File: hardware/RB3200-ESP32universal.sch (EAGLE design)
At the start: 140 parts, among them IC2 7805, IC3 CP2102N-28, T1 BC337, T2 BC337, U1 ESP-WROOM-32, U2 UM18533, U3 ARDUINOR3-BPLACE, X1 USB-MICRO-B-BOTTOM

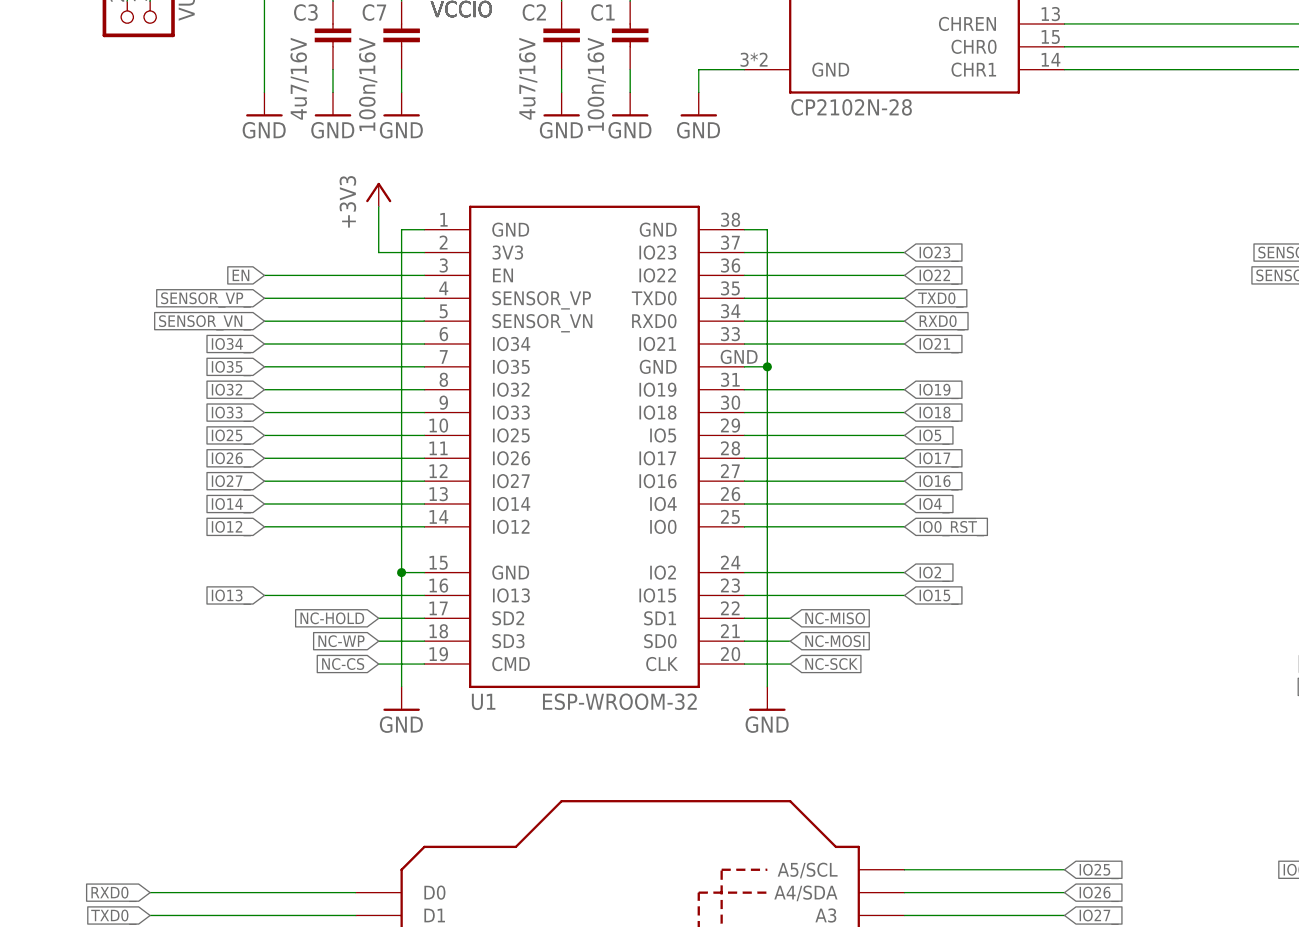
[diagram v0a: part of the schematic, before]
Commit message: Add enable pullup
This solves board flashing issues.
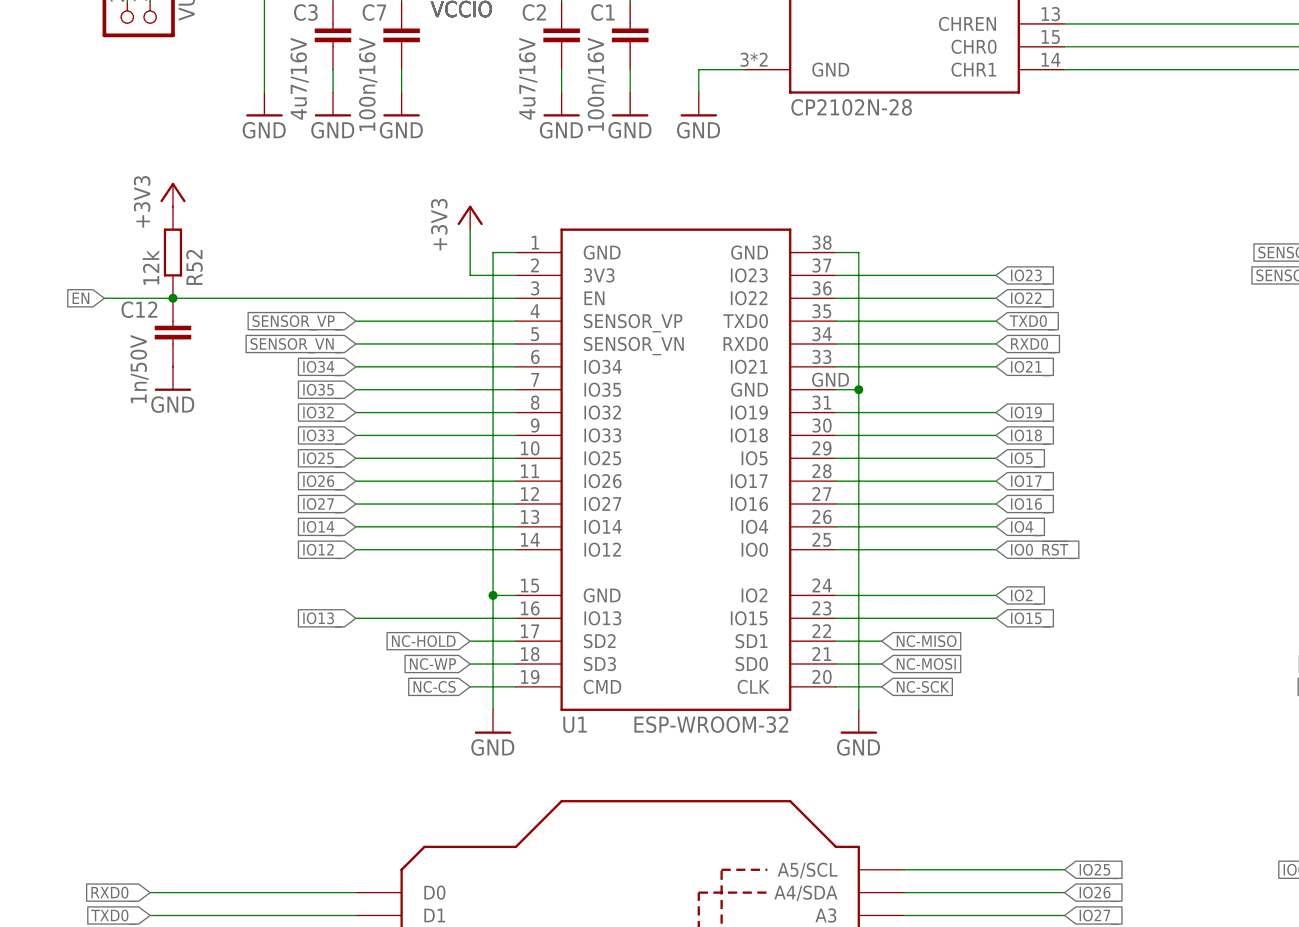
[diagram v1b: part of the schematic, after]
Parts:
- added C12: 1n/50V, rcl_upravena:C-EUC0603
- added R52: 12k, rcl_upravena:R-EU_R0603
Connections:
- net +3V3: now also R52.2
- net EN: now also C12.1, R52.1
- net GND: now also C12.2
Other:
- moved on the sheet: U1

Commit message: Change EN pullup value to simplify BOM
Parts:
- R52: value 12k -> 10k
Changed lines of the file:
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@@
 <grid distance="0.1" unitdist="inch" unit="inch" style="lines" multiple="1" display="no" altdistance="0.01" altunitdist="inch" altunit="inch"/>
 <layers>
-<layer number="1" name="Top" color="4" fill="1" visible="yes" active="no"/>
-<layer number="2" name="Route2" color="1" fill="3" visible="yes" active="no"/>
-<layer number="3" name="Route3" color="4" fill="3" visible="yes" active="no"/>
-<layer number="4" name="Route4" color="1" fill="4" visible="yes" active="no"/>
-<layer number="5" name="Route5" color="4" fill="4" visible="yes" active="no"/>
-<layer number="6" name="Route6" color="1" fill="8" visible="yes" active="no"/>
-<layer number="7" name="Route7" color="4" fill="8" visible="yes" active="no"/>
-<layer number="8" name="Route8" color="1" fill="2" visible="yes" active="no"/>
-<layer number="9" name="Route9" color="4" fill="2" visible="yes" active="no"/>
-<layer number="10" name="Route10" color="1" fill="7" visible="yes" active="no"/>
-<layer number="11" name="Route11" color="4" fill="7" visible="yes" active="no"/>
-<layer number="12" name="Route12" color="1" fill="5" visible="yes" active="no"/>
-<layer number="13" name="Route13" color="4" fill="5" visible="yes" active="no"/>
-<layer number="14" name="Route14" color="1" fill="6" visible="yes" active="no"/>
-<layer number="15" name="Route15" color="4" fill="6" visible="yes" active="no"/>
-<layer number="16" name="Bottom" color="1" fill="1" visible="yes" active="no"/>
-<layer number="17" name="Pads" color="2" fill="1" visible="yes" active="no"/>
-<layer number="18" name="Vias" color="2" fill="1" visible="yes" active="no"/>
-<layer number="19" name="Unrouted" color="6" fill="1" visible="yes" active="no"/>
-<layer number="20" name="Dimension" color="15" fill="1" visible="yes" active="no"/>
-<layer number="21" name="tPlace" color="7" fill="1" visible="yes" active="no"/>
-<layer number="22" name="bPlace" color="7" fill="1" visible="yes" active="no"/>
-<layer number="23" name="tOrigins" color="15" fill="1" visible="yes" active="no"/>
-<layer number="24" name="bOrigins" color="15" fill="1" visible="yes" active="no"/>
-<layer number="25" name="tNames" color="7" fill="1" visible="yes" active="no"/>
-<layer number="26" name="bNames" color="7" fill="1" visible="yes" active="no"/>
-<layer number="27" name="tValues" color="7" fill="1" visible="yes" active="no"/>
-<layer number="28" name="bValues" color="7" fill="1" visible="yes" active="no"/>
+<layer number="1" name="Top" color="4" fill="1" visible="no" active="no"/>
+<layer number="2" name="Route2" color="1" fill="3" visible="no" active="no"/>
+<layer number="3" name="Route3" color="4" fill="3" visible="no" active="no"/>
+<layer number="4" name="Route4" color="1" fill="4" visible="no" active="no"/>
+<layer number="5" name="Route5" color="4" fill="4" visible="no" active="no"/>
+<layer number="6" name="Route6" color="1" fill="8" visible="no" active="no"/>
+<layer number="7" name="Route7" color="4" fill="8" visible="no" active="no"/>
+<layer number="8" name="Route8" color="1" fill="2" visible="no" active="no"/>
+<layer number="9" name="Route9" color="4" fill="2" visible="no" active="no"/>
+<layer number="10" name="Route10" color="1" fill="7" visible="no" active="no"/>
+<layer number="11" name="Route11" color="4" fill="7" visible="no" active="no"/>
+<layer number="12" name="Route12" color="1" fill="5" visible="no" active="no"/>
+<layer number="13" name="Route13" color="4" fill="5" visible="no" active="no"/>
+<layer number="14" name="Route14" color="1" fill="6" visible="no" active="no"/>
+<layer number="15" name="Route15" color="4" fill="6" visible="no" active="no"/>
+<layer number="16" name="Bottom" color="1" fill="1" visible="no" active="no"/>
+<layer number="17" name="Pads" color="2" fill="1" visible="no" active="no"/>
+<layer number="18" name="Vias" color="2" fill="1" visible="no" active="no"/>
+<layer number="19" name="Unrouted" color="6" fill="1" visible="no" active="no"/>
+<layer number="20" name="Dimension" color="15" fill="1" visible="no" active="no"/>
+<layer number="21" name="tPlace" color="7" fill="1" visible="no" active="no"/>
+<layer number="22" name="bPlace" color="7" fill="1" visible="no" active="no"/>
+<layer number="23" name="tOrigins" color="15" fill="1" visible="no" active="no"/>
+<layer number="24" name="bOrigins" color="15" fill="1" visible="no" active="no"/>
+<layer number="25" name="tNames" color="7" fill="1" visible="no" active="no"/>
+<layer number="26" name="bNames" color="7" fill="1" visible="no" active="no"/>
+<layer number="27" name="tValues" color="7" fill="1" visible="no" active="no"/>
+<layer number="28" name="bValues" color="7" fill="1" visible="no" active="no"/>
 <layer number="29" name="tStop" color="7" fill="3" visible="no" active="no"/>
 <layer number="30" name="bStop" color="7" fill="6" visible="no" active="no"/>
@@
 <layer number="35" name="tGlue" color="7" fill="4" visible="no" active="no"/>
 <layer number="36" name="bGlue" color="7" fill="5" visible="no" active="no"/>
-<layer number="37" name="tTest" color="7" fill="1" visible="yes" active="no"/>
-<layer number="38" name="bTest" color="7" fill="1" visible="yes" active="no"/>
+<layer number="37" name="tTest" color="7" fill="1" visible="no" active="no"/>
+<layer number="38" name="bTest" color="7" fill="1" visible="no" active="no"/>
 <layer number="39" name="tKeepout" color="4" fill="11" visible="no" active="no"/>
 <layer number="40" name="bKeepout" color="1" fill="11" visible="no" active="no"/>
@@
 <layer number="44" name="Drills" color="7" fill="1" visible="no" active="no"/>
 <layer number="45" name="Holes" color="7" fill="1" visible="no" active="no"/>
-<layer number="46" name="Milling" color="3" fill="1" visible="yes" active="no"/>
-<layer number="47" name="Measures" color="7" fill="1" visible="yes" active="no"/>
-<layer number="48" name="Document" color="7" fill="1" visible="yes" active="no"/>
-<layer number="49" name="Reference" color="7" fill="1" visible="yes" active="no"/>
-<layer number="50" name="dxf" color="7" fill="1" visible="yes" active="no"/>
-<layer number="51" name="tDocu" color="7" fill="1" visible="yes" active="no"/>
-<layer number="52" name="bDocu" color="7" fill="1" visible="yes" active="no"/>
-<layer number="53" name="tGND_GNDA" color="7" fill="9" visible="yes" active="no"/>
-<layer number="54" name="bGND_GNDA" color="1" fill="9" visible="yes" active="no"/>
-<layer number="55" name="tPotisk" color="7" fill="1" visible="yes" active="no"/>
-<layer number="56" name="wert" color="7" fill="1" visible="yes" active="no"/>
-<layer number="57" name="tCAD" color="7" fill="1" visible="yes" active="no"/>
-<layer number="58" name="bNC" color="7" fill="1" visible="yes" active="no"/>
-<layer number="59" name="tCarbon" color="7" fill="1" visible="yes" active="no"/>
-<layer number="60" name="bCarbon" color="7" fill="1" visible="yes" active="no"/>
-<layer number="61" name="stand" color="7" fill="1" visible="yes" active="no"/>
+<layer number="46" name="Milling" color="3" fill="1" visible="no" active="no"/>
+<layer number="47" name="Measures" color="7" fill="1" visible="no" active="no"/>
+<layer number="48" name="Document" color="7" fill="1" visible="no" active="no"/>
+<layer number="49" name="Reference" color="7" fill="1" visible="no" active="no"/>
+<layer number="50" name="dxf" color="7" fill="1" visible="no" active="no"/>
+<layer number="51" name="tDocu" color="7" fill="1" visible="no" active="no"/>
+<layer number="52" name="bDocu" color="7" fill="1" visible="no" active="no"/>
+<layer number="53" name="tGND_GNDA" color="7" fill="9" visible="no" active="no"/>
+<layer number="54" name="bGND_GNDA" color="1" fill="9" visible="no" active="no"/>
+<layer number="55" name="tPotisk" color="7" fill="1" visible="no" active="no"/>
+<layer number="56" name="wert" color="7" fill="1" visible="no" active="no"/>
+<layer number="57" name="tCAD" color="7" fill="1" visible="no" active="no"/>
+<layer number="58" name="bNC" color="7" fill="1" visible="no" active="no"/>
+<layer number="59" name="tCarbon" color="7" fill="1" visible="no" active="no"/>
+<layer number="60" name="bCarbon" color="7" fill="1" visible="no" active="no"/>
+<layer number="61" name="stand" color="7" fill="1" visible="no" active="no"/>
 <layer number="90" name="Modules" color="5" fill="1" visible="no" active="yes"/>
 <layer number="91" name="Nets" color="2" fill="1" visible="yes" active="yes"/>
@@
 <part name="+3V15" library="supply1" deviceset="+3V3" device=""/>
 <part name="FRAME2" library="frames" deviceset="A3L-LOC" device=""/>
-<part name="R52" library="rcl_upravena" deviceset="R-EU_" device="R0603" value="12k"/>
+<part name="R52" library="rcl_upravena" deviceset="R-EU_" device="R0603" value="10k"/>
 <part name="C12" library="rcl_upravena" deviceset="C-EU" device="C0603" value="1n/50V"/>
 <part name="GND32" library="supply1" deviceset="GND" device=""/>

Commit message: Add order codes to the components.
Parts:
- !CTS, !DCD, !DSR, !DTR, !RESET, !RTS, !SUSPEND, CHR0, CHR1, CHREN, IO0/TXLED, IO1/RXLED, IO2/RS485, IO3/WAKEUP, IO4, IO5, IO6, RI/CLK, RXD, SUSPEND, TXD: DIGIKEY (none) -> WM14724-ND; FARNELL (none) -> 1756963; MOUSER (none) -> 538-90120-0761; RS (none) -> 863-2706
- +5V, SERVOS: DIGIKEY (none) -> A122662-ND; FARNELL (none) -> 1248162; MOUSER (none) -> 571-826942-6; RS (none) -> 681-2953
- B1, B2: DIGIKEY (none) -> CKN1574TR-ND; FARNELL (none) -> 2079520; MOUSER (none) -> 611-PTS635SL43SMTRLF; RS (none) -> 135-9609
- C1, C11, C20, C21, C6, C7: DIGIKEY (none) -> 732-7478-1-ND; FARNELL (none) -> 2533923RL; MOUSER (none) -> 710-885012105001; RS (none) -> 839-1622
- C10, C67, C70, C8, C9: DIGIKEY (none) -> 1276-2970-2-ND; FARNELL (none) -> 2320854; MOUSER (none) -> 963-EMK212B7475KG-T; RS (none) -> 766-1037
- C12: DIGIKEY (none) -> 399-1082-1-ND; FARNELL (none) -> 1414608; MOUSER (none) -> 80-C0603C102K5R; RS (none) -> 264-4551
- C2, C3, C4, C5: DIGIKEY (none) -> 478-1253-1-ND; FARNELL (none) -> 9227784; MOUSER (none) -> 06034D475KAT2A; RS (none) -> 698-3248
- C37: DIGIKEY (none) -> 493-6629-1-ND; FARNELL (none) -> 9692045; MOUSER (none) -> 140-REA331M1CBK0811P; RS (none) -> 707-5840
- EN, JP36, JP38, VUSB: DIGIKEY (none) -> 3M9457-02-ND; FARNELL (none) -> 2396217; MOUSER (none) -> 517-9611026404AR; RS (none) -> 827-7775
- IC2: DIGIKEY (none) -> 1016-1538-5-ND; FARNELL (none) -> 9756078; MOUSER (none) -> 701-SP7805V-L; RS (none) -> 769-5466
- IC3: DIGIKEY (none) -> 336-3694-ND; FARNELL (none) -> 2577279; MOUSER (none) -> 634-CP2102NA01GQFN28; RS (none) -> 526-8841
- JP1: DIGIKEY (none) -> WM50014-12-ND; FARNELL (none) -> 1593418; MOUSER (none) -> 538-22-28-4120; RS (none) -> 821-5689
- JP11: DIGIKEY (none) -> A122911-ND; FARNELL (none) -> 1248147; MOUSER (none) -> 571-826926-8; RS (none) -> 669-5339
- JP2, JP3, PWR_1: DIGIKEY (none) -> WM8148-ND; FARNELL (none) -> 9733663; MOUSER (none) -> 538-90131-0772; RS (none) -> 670-3500
- JP5: DIGIKEY (none) -> 0901200134-ND; FARNELL (none) -> 2356164; MOUSER (none) -> 538-90120-0134; RS (none) -> 670-5060
- JP6, JP7, PWR_2: DIGIKEY (none) -> WM8150-ND; FARNELL (none) -> 2356142; MOUSER (none) -> 538-90131-0774; RS (none) -> 670-3512
- LED0N, LED1N, LED2N, LED3N, LED4N, LED5N: DIGIKEY (none) -> 160-1447-2-ND; FARNELL (none) -> 2322071; MOUSER (none) -> 859-LTST-C191KRKT; RS (none) -> 127-8415
- LED0P, LED1P, LED2P, LED3P, LED4P, LED5P, LED_3V3, LED_3V3_USB: DIGIKEY (none) -> 872-1799; FARNELL (none) -> 2293494; MOUSER (none) -> 859-LTST-C191KGKT; RS (none) -> 872-1799
- LED1, LED2, LED3: DIGIKEY (none) -> 732-4981-1-ND; FARNELL (none) -> 2322074; MOUSER (none) -> 710-150060YS75000; RS (none) -> 815-4219
- LEDS, VCC, VCCIO: DIGIKEY (none) -> A122915-ND; FARNELL (none) -> 1248159; MOUSER (none) -> 571-826942-3; RS (none) -> 360-6443
- PWR: DIGIKEY (none) -> 277-5953-ND; FARNELL (none) -> 2490945; MOUSER (none) -> 651-1890963; RS (none) -> 804-5118
- R1, R2, R26, R3, R36, R38, R40, R42, R44, R46, R48: DIGIKEY (none) -> 311-470HRCT-ND; FARNELL (none) -> 9238441; MOUSER (none) -> 603-RC0603FR-07470RL; RS (none) -> 504-7341
- R10, R11, R12, R13, R14, R15, R16, R17, R18, R19, R20, R21, R22, R23, R24, R25, R27, R28, R29, R30, R31, R32, R33, R34, R6, R7, R8, R9: DIGIKEY (none) -> 311-180HRCT-ND; FARNELL (none) -> 9238395; MOUSER (none) -> 603-RC0603FR-07180RL; RS (none) -> 504-9937
- R35, R4, R5, R50, R51, R52: DIGIKEY (none) -> 311-10KGRCT-ND; FARNELL (none) -> 9238603; MOUSER (none) -> 603-RC0603FR-0710KL; RS (none) -> 504-8934
- R37: DIGIKEY (none) -> 311-100KHRCT-ND; FARNELL (none) -> 9238727; MOUSER (none) -> 603-RC0603FR-07100KL; RS (none) -> 504-8940
- R39, R41, R43, R45, R47, R49: DIGIKEY (none) -> 311-680HRCT-ND; FARNELL (none) -> 9238468; MOUSER (none) -> 603-RC0603FR-13680RL
- T1, T2: DIGIKEY (none) -> 1727-2919-1-ND; FARNELL (none) -> 1081224; MOUSER (none) -> 771-BC817-40-T/R; RS (none) -> 216-9410
- U1: DIGIKEY (none) -> 1738-1294-ND
- U2: DIGIKEY (none) -> 296-17580-1-ND; FARNELL (none) -> 1135395; MOUSER (none) -> 595-TPS73033DBVR; RS (none) -> 620-1401
- USB: DIGIKEY (none) -> 732-5318-ND; FARNELL (none) -> 2356157; MOUSER (none) -> 710-61300511121; RS (none) -> 828-1597
- X1: DIGIKEY (none) -> WM17141CT-ND; FARNELL (none) -> 1568026; MOUSER (none) -> 538-47346-0001; RS (none) -> 702-5475

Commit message: Tweak BOM according to #4
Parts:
- C1, C11, C20, C21, C6, C7: FARNELL 2533923RL -> 2533923; RS 839-1622 -> 788-2871
- C10, C67, C70, C8, C9: DIGIKEY 1276-2970-2-ND -> 1276-2970-1-ND
- IC3: MANUFACTURER (none) -> Silicon Labs; MPN (none) -> CP2102
- JP5: DIGIKEY 0901200134-ND -> (none)
- LED0N, LED1N, LED2N, LED3N, LED4N, LED5N: DIGIKEY 160-1447-2-ND -> 160-1447-1-ND
- LED0P, LED1P, LED2P, LED3P, LED4P, LED5P, LED_3V3, LED_3V3_USB: DIGIKEY 872-1799 -> 160-1446-1-ND
- R1, R2, R26, R3, R36, R38, R40, R42, R44, R46, R48: RS 504-7341 -> 566-547
- R10, R11, R12, R13, R14, R15, R16, R17, R18, R19, R20, R21, R22, R23, R24, R25, R27, R28, R29, R30, R31, R32, R33, R34, R6, R7, R8, R9: RS 504-9937 -> 566-412
- R35, R4, R5, R50, R51, R52: RS 504-8934 -> 213-2418
- R37: RS 504-8940 -> 566-787
- U1: MANUFACTURER (none) -> Espressif Systems; MPN (none) -> ESP32-WROMM-32
- U2: MANUFACTURER (none) -> Texas Instruments; MPN (none) -> TPS73033DBVT
